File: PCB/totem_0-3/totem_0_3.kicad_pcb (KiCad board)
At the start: 2 copper layers, 258.7 x 94.4 mm, 178 parts, among them J1 MJ-4PP-9, J2 MJ-4PP-9, U1 xiao-ble, U2 xiao-ble

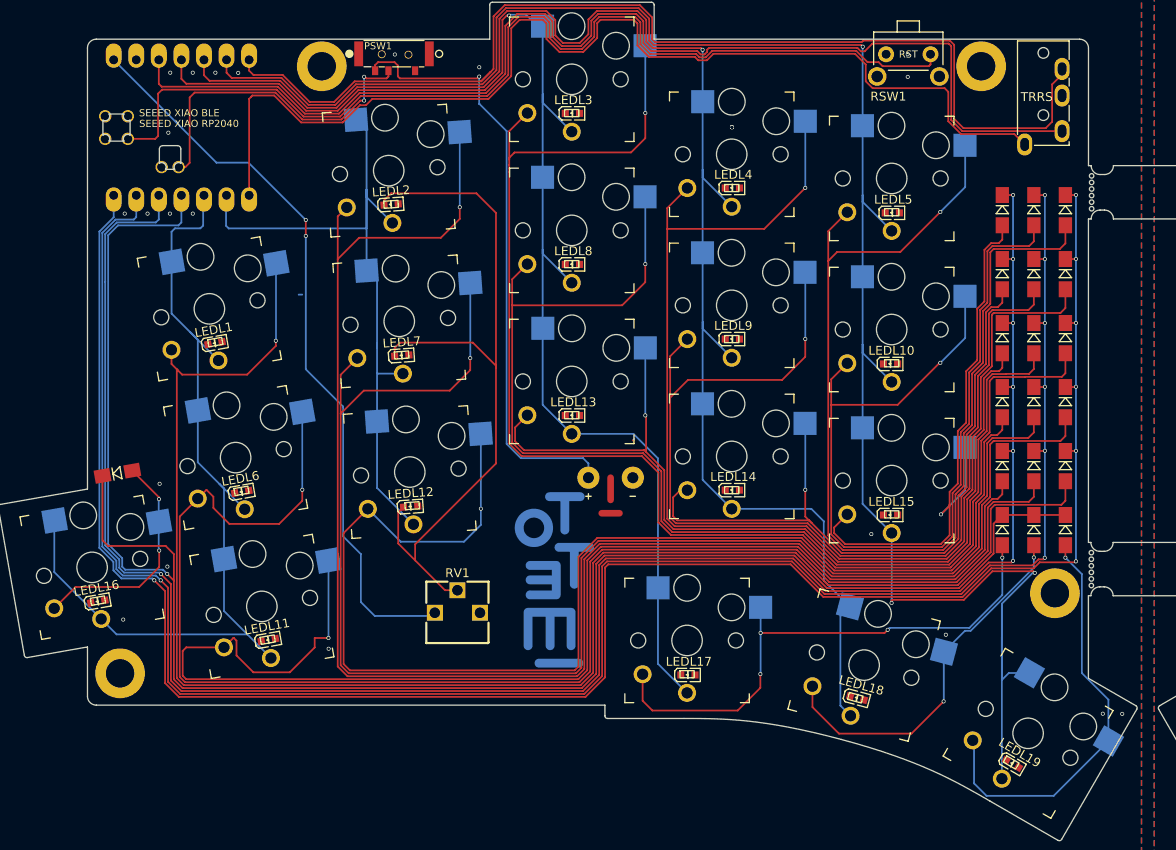
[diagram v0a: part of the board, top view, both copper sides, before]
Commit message: Adding backlight shematics, wiring left hand, wip
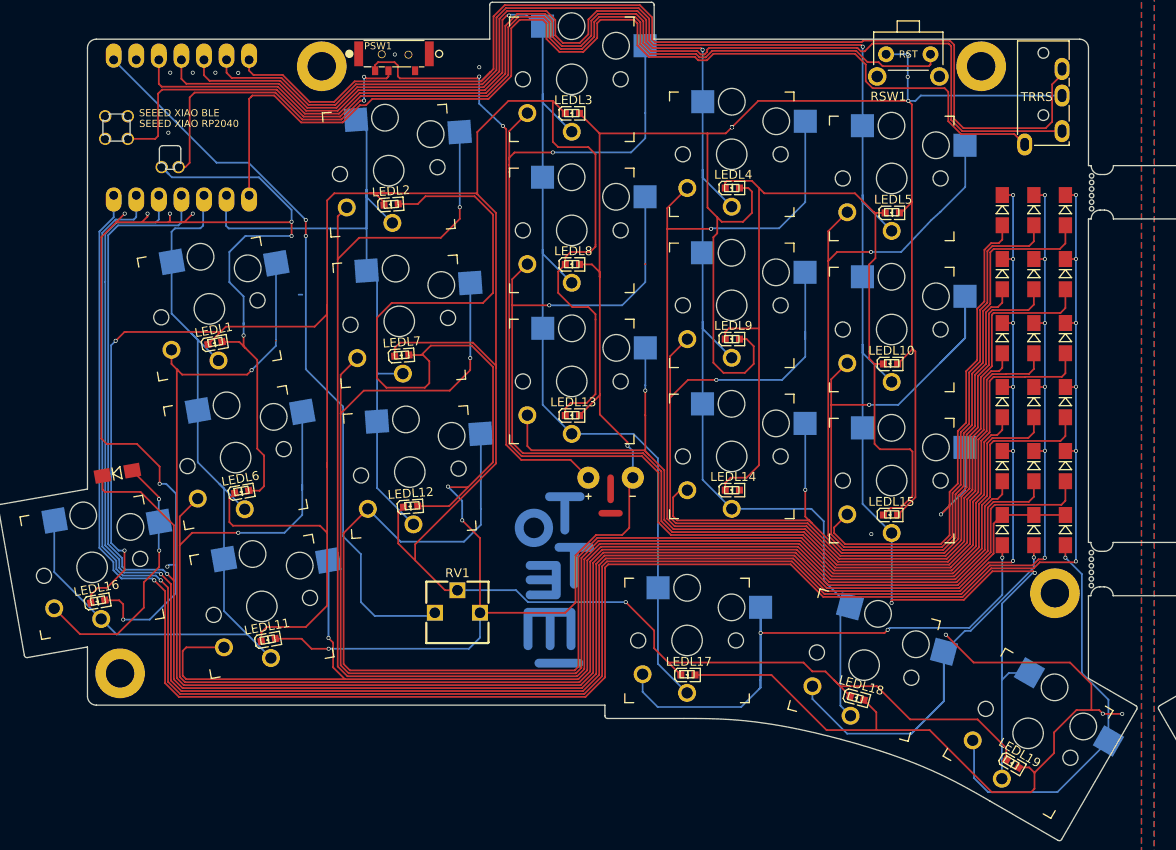
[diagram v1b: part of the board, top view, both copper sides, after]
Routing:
- net GND_L: track 0.72 -> 605.0 mm, vias 39 -> 46
- net Net-(LEDL1-A): track 84.2 -> 472.0 mm, vias 0 -> 3
- net Net-(DL11-A): track 148.9 -> 137.3 mm
- net Net-(DL18-A): track 42.0 -> 52.2 mm, vias 2 -> 1
- net Net-(DL10-A): track 98.9 -> 107.5 mm
- net Net-(DL17-A): track 61.4 -> 69.8 mm, vias 4 -> 3
- net Net-(DL16-A): track 25.9 -> 29.9 mm
- net Net-(DL6-A): track 166.4 -> 168.1 mm
- net Net-(DL13-A): track 99.7 -> 97.9 mm
- net ROW3_L: track 207.4 -> 205.9 mm
- net Net-(DL4-A): track 136.7 -> 137.7 mm
- net VBAT_L: track 68.4 -> 67.6 mm, vias 1 -> 2
- net Net-(DL9-A): track 116.8 -> 117.6 mm
- net Net-(DL19-A): track 47.7 -> 47.0 mm
- net Net-(DL12-A): vias 1 -> 0
